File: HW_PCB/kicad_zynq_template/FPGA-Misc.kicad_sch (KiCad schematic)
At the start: 1 part, among them U2 XA7Z020-1CLG400I

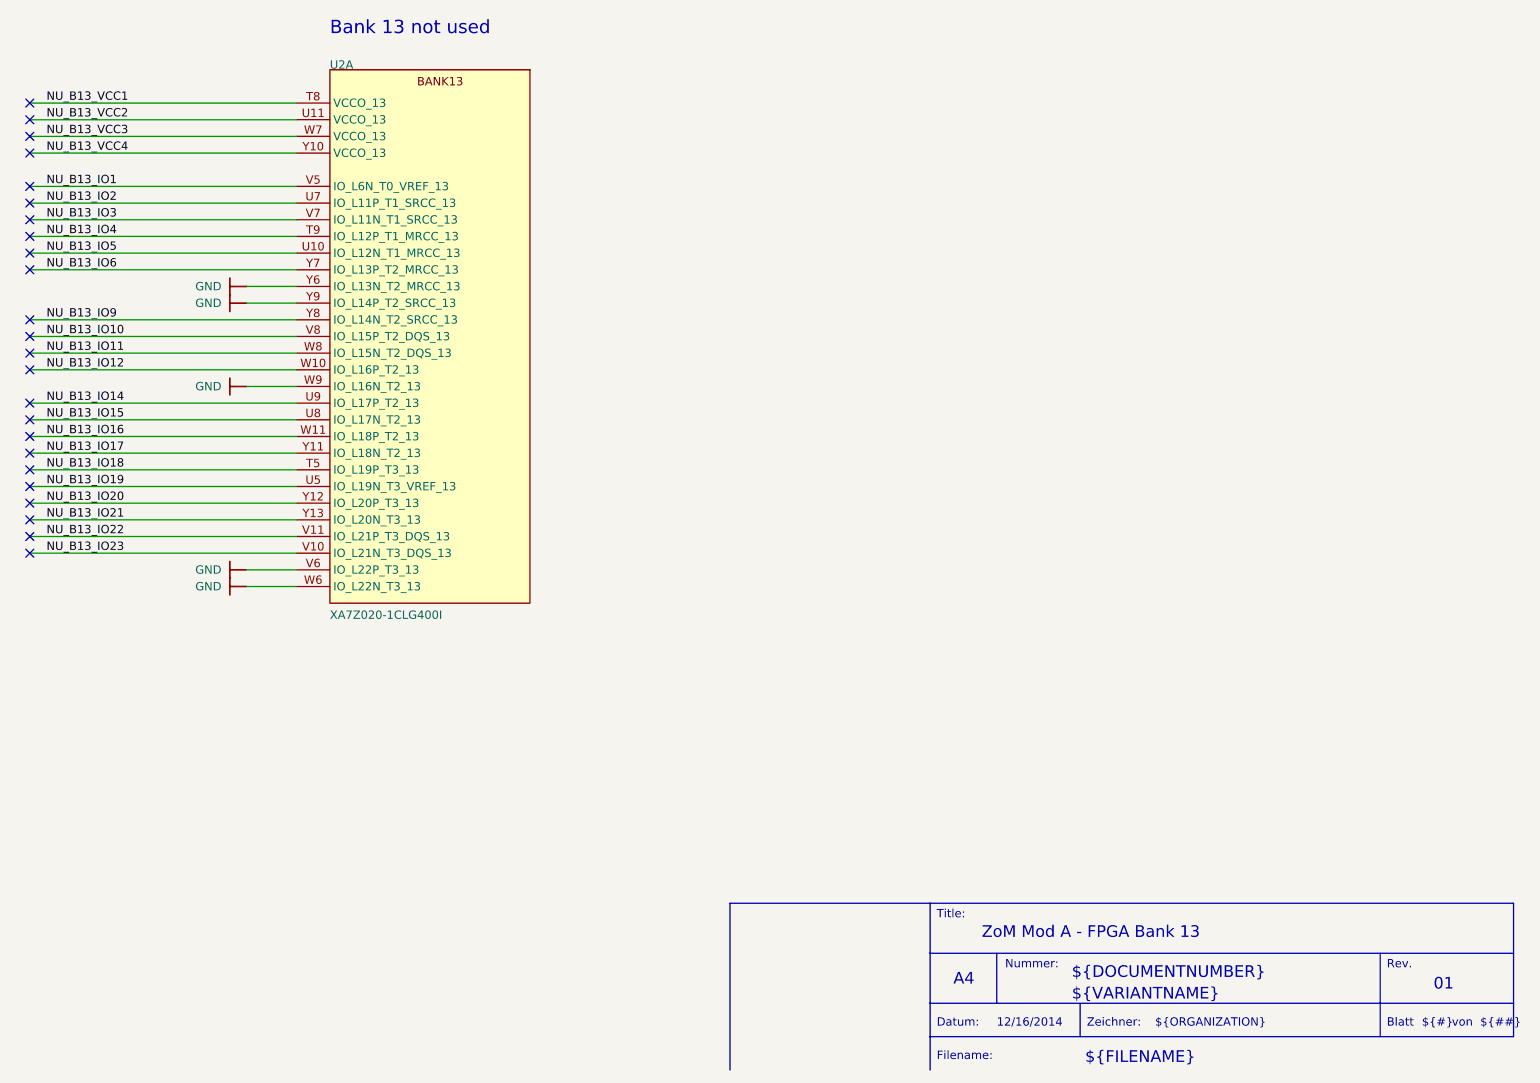
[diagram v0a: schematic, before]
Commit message: pcbs tidied up
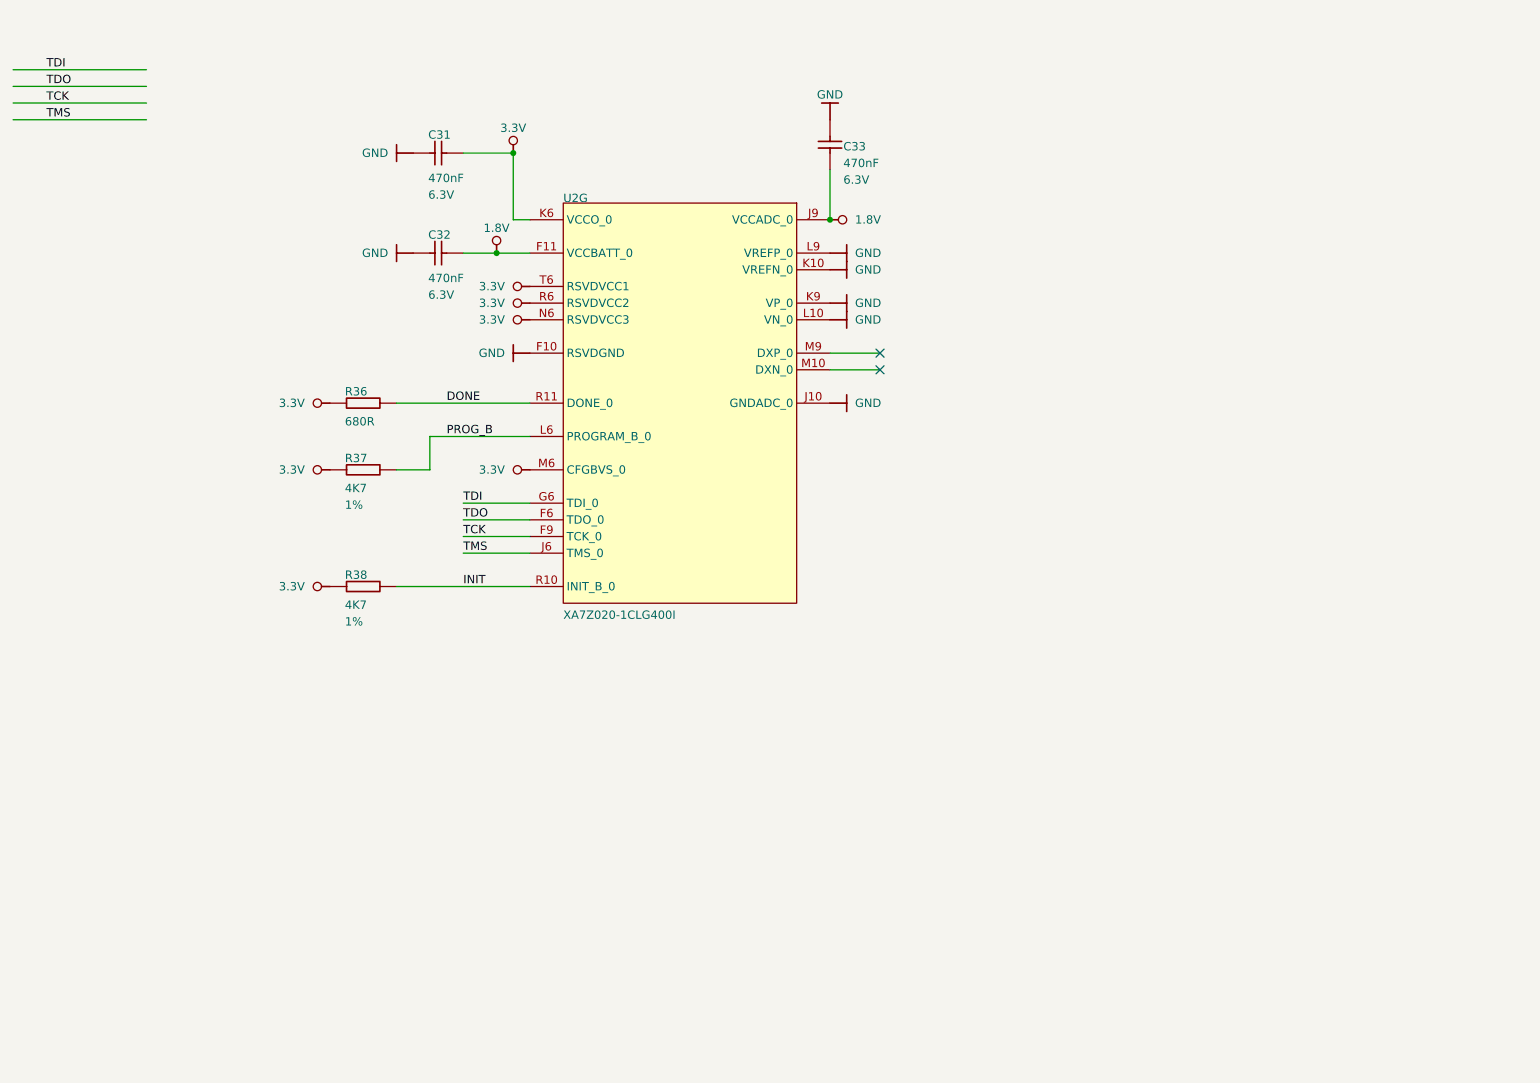
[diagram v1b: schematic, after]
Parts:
- removed U2: XA7Z020-1CLG400I, BGA400C80P20X20_1700X1700X160N, symbol TE0719-altium-import:B13_0_XC7Z020-2CLG400C
- added C31: 470nF, symbol TE0719-altium-import:FPGA-Misc_1_CAP-NP
- added C32: 470nF, CAPC0603X33N, symbol TE0719-altium-import:FPGA-Misc_1_CAP-NP
- added C33: 470nF, CAPC0603X33N, symbol TE0719-altium-import:FPGA-Misc_0_CAP-NP
- added R36: 680R, RESC1005X40N, symbol TE0719-altium-import:FPGA-Misc_1_RES
- added R37: 4K7, RESC0603X26N, symbol TE0719-altium-import:FPGA-Misc_3_RES
- added R38: 4K7, symbol TE0719-altium-import:FPGA-Misc_3_RES
- added U2: XA7Z020-1CLG400I, BGA400C80P20X20_1700X1700X160N, symbol TE0719-altium-import:FPGA-Misc_0_XC7Z020-2CLG400C
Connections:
- net GND: now also C31.1, C32.1, C33.1, U2.F10 (RSVDGND), U2.J10 (GNDADC_0), U2.K10 (VREFN_0), U2.K9 (VP_0), U2.L10 (VN_0), U2.L9 (VREFP_0)
- new net 1.8V: C32.2, C33.2, U2.F11 (VCCBATT_0), U2.J9 (VCCADC_0)
- new net 3.3V: C31.2, R36.1, R37.2, R38.2, U2.K6 (VCCO_0), U2.M6 (CFGBVS_0), U2.N6 (RSVDVCC3), U2.R6 (RSVDVCC2), U2.T6 (RSVDVCC1)
- new net DONE: R36.2, U2.R11 (DONE_0)
- new net INIT: R38.1, U2.R10 (INIT_B_0)
- new net PROG_B: R37.1, U2.L6 (PROGRAM_B_0)
- new net TCK: U2.F9 (TCK_0)
- new net TDI: U2.G6 (TDI_0)
- new net TDO: U2.F6 (TDO_0)
- new net TMS: U2.J6 (TMS_0)
- no-connect marks 24 -> 2
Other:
- note removed: "${##}"
- note removed: "${#}"
- note removed: "${DOCUMENTNUMBER}"
- note removed: "${FILENAME}"
- note removed: "${ISSUE_DATE}"
- note removed: "${ORGANIZATION}"
- note removed: "${REVISION}"
- note removed: "${TITLE}"
- note removed: "${VARIANTNAME}"
- note removed: "A4"
- note removed: "Bank 13 not used"
- note removed: "Blatt"
- note removed: "Datum:"
- note removed: "Filename:"
- note removed: "Nummer:"
- note removed: "Rev."
- note removed: "Title:"
- note removed: "Zeichner:"
- note removed: "von"
- title: ZoM Mod A - FPGA Bank 13 -> ZoM Mod A - FPGA MIsc
